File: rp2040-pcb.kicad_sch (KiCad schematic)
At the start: 10 parts

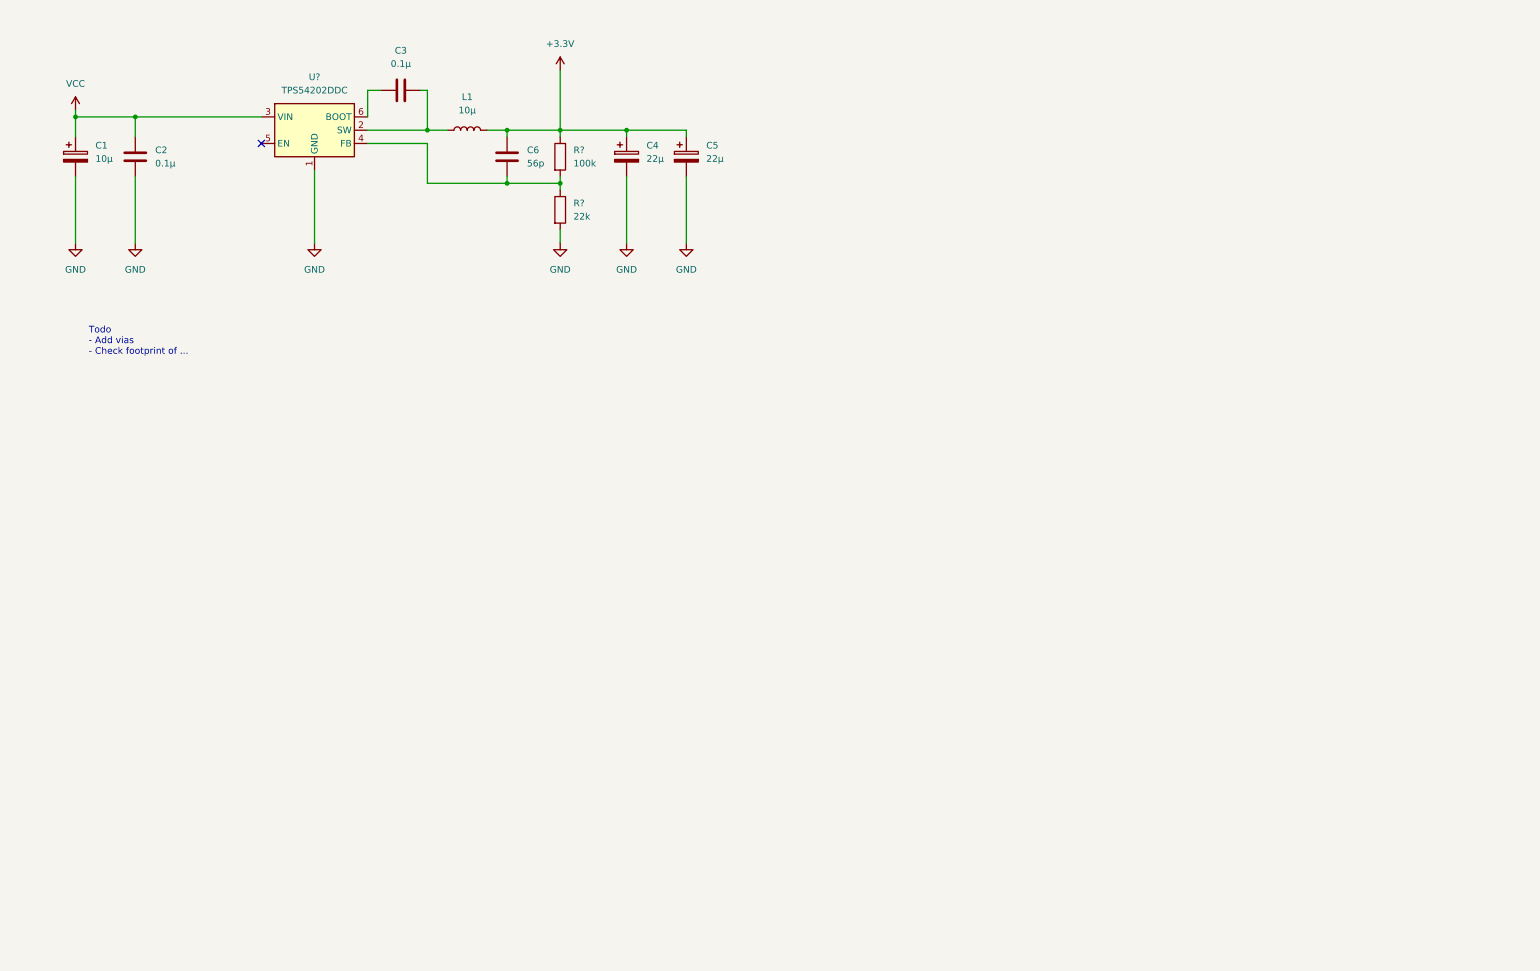
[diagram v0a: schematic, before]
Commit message: Added SPI-memory.
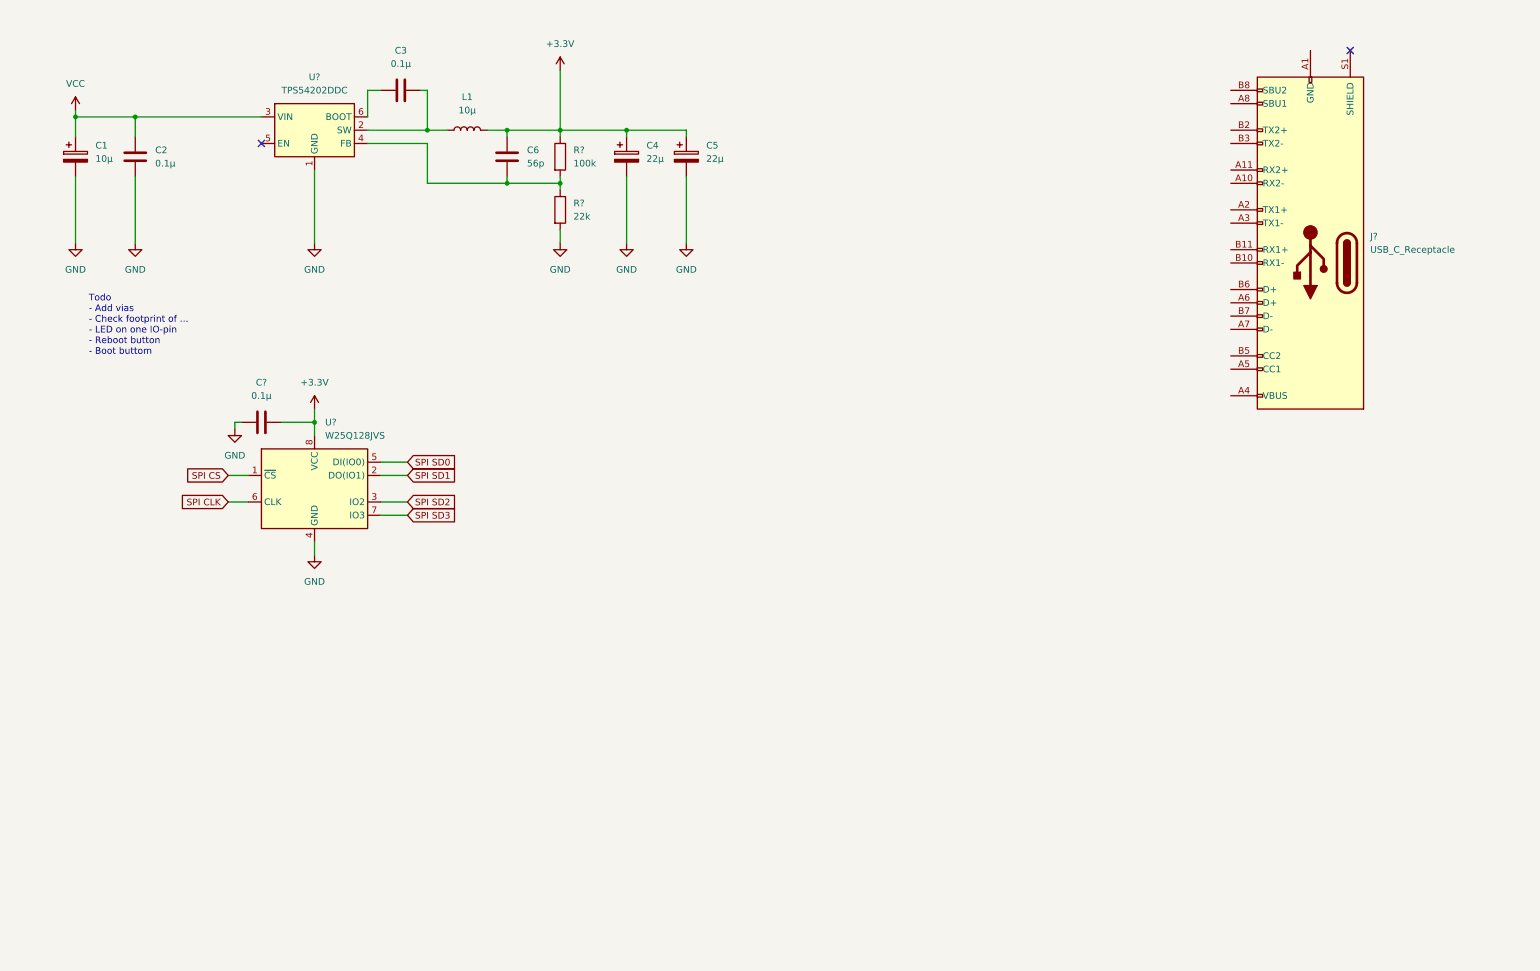
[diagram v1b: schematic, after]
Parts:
- added C?: 0.1µ, Capacitor_SMD:C_0805_2012Metric, symbol Device:C
- added J?: USB_C_Receptacle, symbol Connector:USB_C_Receptacle
- added U?: W25Q128JVS, Package_SO:SOIC-8_5.23x5.23mm_P1.27mm, symbol Memory_Flash:W25Q128JVS
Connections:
- net +3.3V: now also C?.2, U?.8 (VCC)
- net GND: now also C?.1, U?.4 (GND)
- new net: J?.A1 (GND), J?.A12 (GND), J?.B1 (GND), J?.B12 (GND)
- new net: J?.A4 (VBUS), J?.A9 (VBUS), J?.B4 (VBUS), J?.B9 (VBUS)
- new net SPI CLK: U?.6 (CLK)
- new net SPI CS: U?.1 (~{CS})
- new net SPI SD0: U?.5 (DI(IO0))
- new net SPI SD1: U?.2 (DO(IO1))
- new net SPI SD2: U?.3 (IO2)
- new net SPI SD3: U?.7 (IO3)
- no-connect marks 1 -> 2
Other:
- note added: "Todo - Add vias - Check footprint of ... - LED on one IO-pin - Reboot button - Boot buttom"
- note removed: "Todo - Add vias - Check footprint of ..."

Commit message: Added USB, RP2040 and decoupling caps.
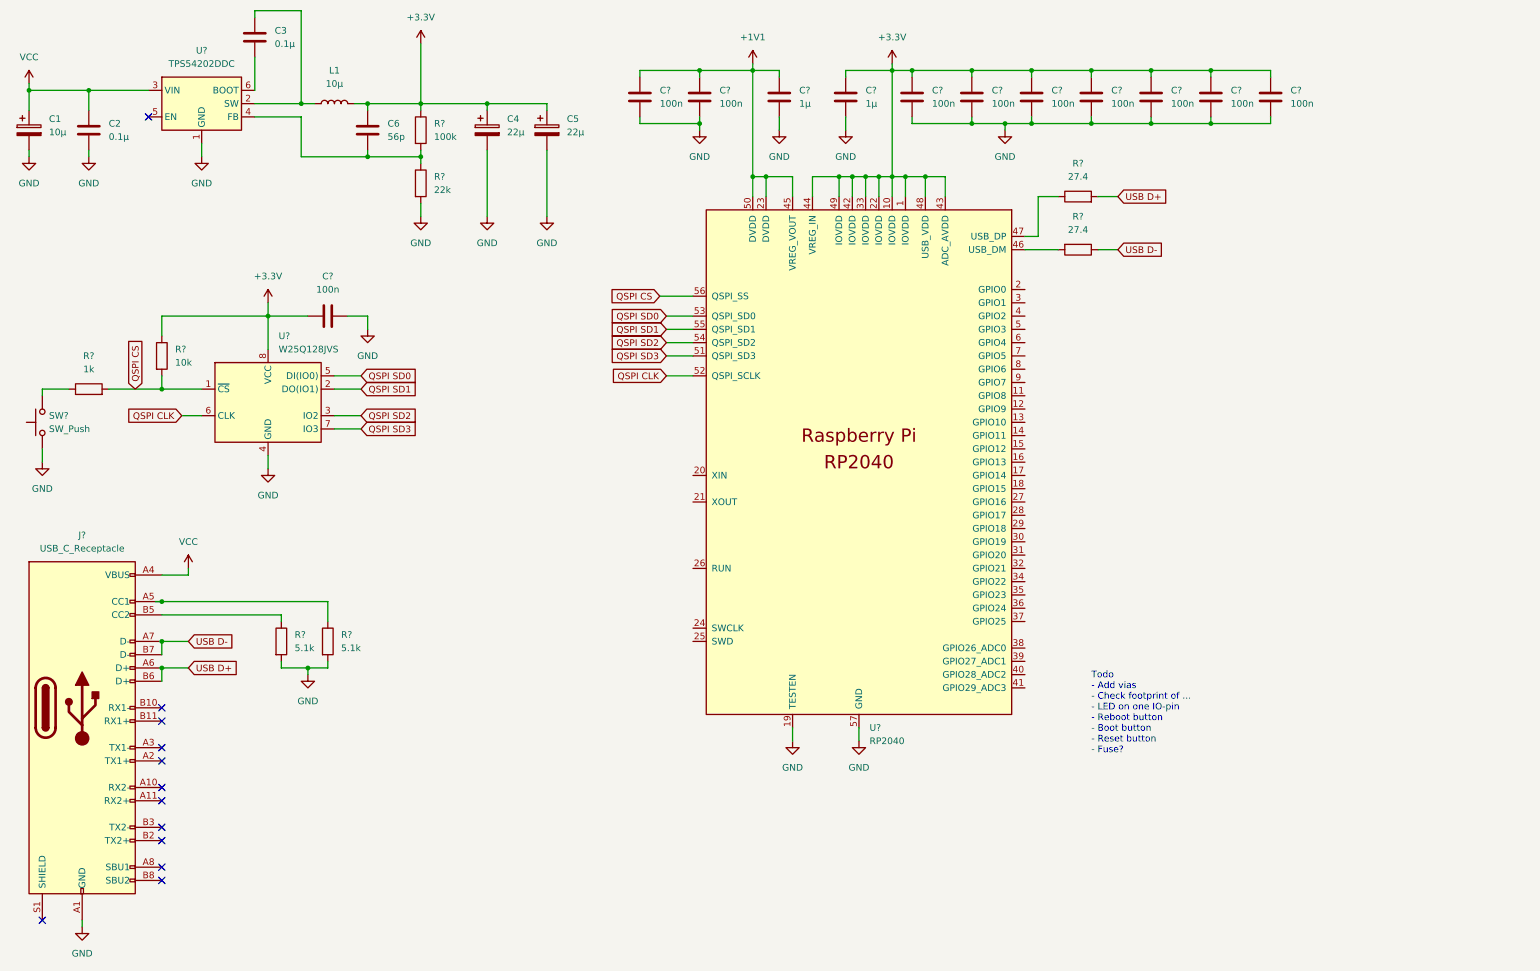
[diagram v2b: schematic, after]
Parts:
- added C? (x2): 1µ, Capacitor_SMD:C_0805_2012Metric, symbol Device:C
- added C? (x9): 100n, Capacitor_SMD:C_0805_2012Metric, symbol Device:C
- added R? (x2): 27.4, symbol Device:R
- added R?: 1k, symbol Device:R
- added R? (x2): 5.1k, symbol Device:R
- added R?: 10k, symbol Device:R
- added SW?: SW_Push, symbol Switch:SW_Push
- added U?: RP2040, RP2040_minimal:RP2040-QFN-56, symbol MCU_RaspberryPi_RP2040:RP2040
- C?: value 0.1µ -> 100n
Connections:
- net +3.3V: now also C?.1, C?.1, C?.1, C?.1, C?.1, C?.1, C?.1, C?.1, R?.1, U?.1 (IOVDD), U?.10 (IOVDD), U?.22 (IOVDD), U?.33 (IOVDD), U?.42 (IOVDD), U?.43 (ADC_AVDD), U?.44 (VREG_IN), U?.48 (USB_VDD), U?.49 (IOVDD)
- net GND: now also J?.A1 (GND), J?.A12 (GND), J?.B1 (GND), J?.B12 (GND), C?.2, C?.2, C?.2, C?.2, C?.2, C?.2, C?.2, C?.2, C?.2, C?.2, C?.2, R?.2, R?.2, SW?.1, U?.19 (TESTEN), U?.57 (GND)
- net VCC: now also J?.A4 (VBUS), J?.A9 (VBUS), J?.B4 (VBUS), J?.B9 (VBUS)
- net at J?.A5 (CC1): now also R?.1
- net USB D+: now reaches J?.A6 (D+)
- net USB D+: now also J?.B6 (D+), R?.2
- net USB D-: now reaches J?.A7 (D-)
- net USB D-: now also J?.B7 (D-), R?.1
- net at J?.B5 (CC2): now also R?.1
- net SPI CLK renamed QSPI CLK
- net QSPI CLK: now also U?.52 (QSPI_SCLK)
- net SPI CS renamed QSPI CS
- net QSPI CS: now also R?.2, R?.2, U?.56 (QSPI_SS)
- net SPI SD0 renamed QSPI SD0
- net QSPI SD0: now also U?.53 (QSPI_SD0)
- net SPI SD1 renamed QSPI SD1
- net QSPI SD1: now also U?.55 (QSPI_SD1)
- net SPI SD2 renamed QSPI SD2
- net QSPI SD2: now also U?.54 (QSPI_SD2)
- net SPI SD3 renamed QSPI SD3
- net QSPI SD3: now also U?.51 (QSPI_SD3)
- new net: R?.1, SW?.2
- new net: R?.1, U?.47 (USB_DP)
- new net: R?.2, U?.46 (USB_DM)
- new net +1V1: C?.1, C?.1, C?.1, U?.23 (DVDD), U?.45 (VREG_VOUT), U?.50 (DVDD)
- no-connect marks 2 -> 12
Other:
- note added: "Todo - Add vias - Check footprint of ... - LED on one IO-pin - Reboot button - Boot button - Reset button - Fuse?"
- note removed: "Todo - Add vias - Check footprint of ... - LED on one IO-pin - Reboot button - Boot buttom"
- moved on the sheet: C1, C2, C3, C4, C5, C6, C?, J?, L1, R?, U?

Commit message: Added IO-header-pins.
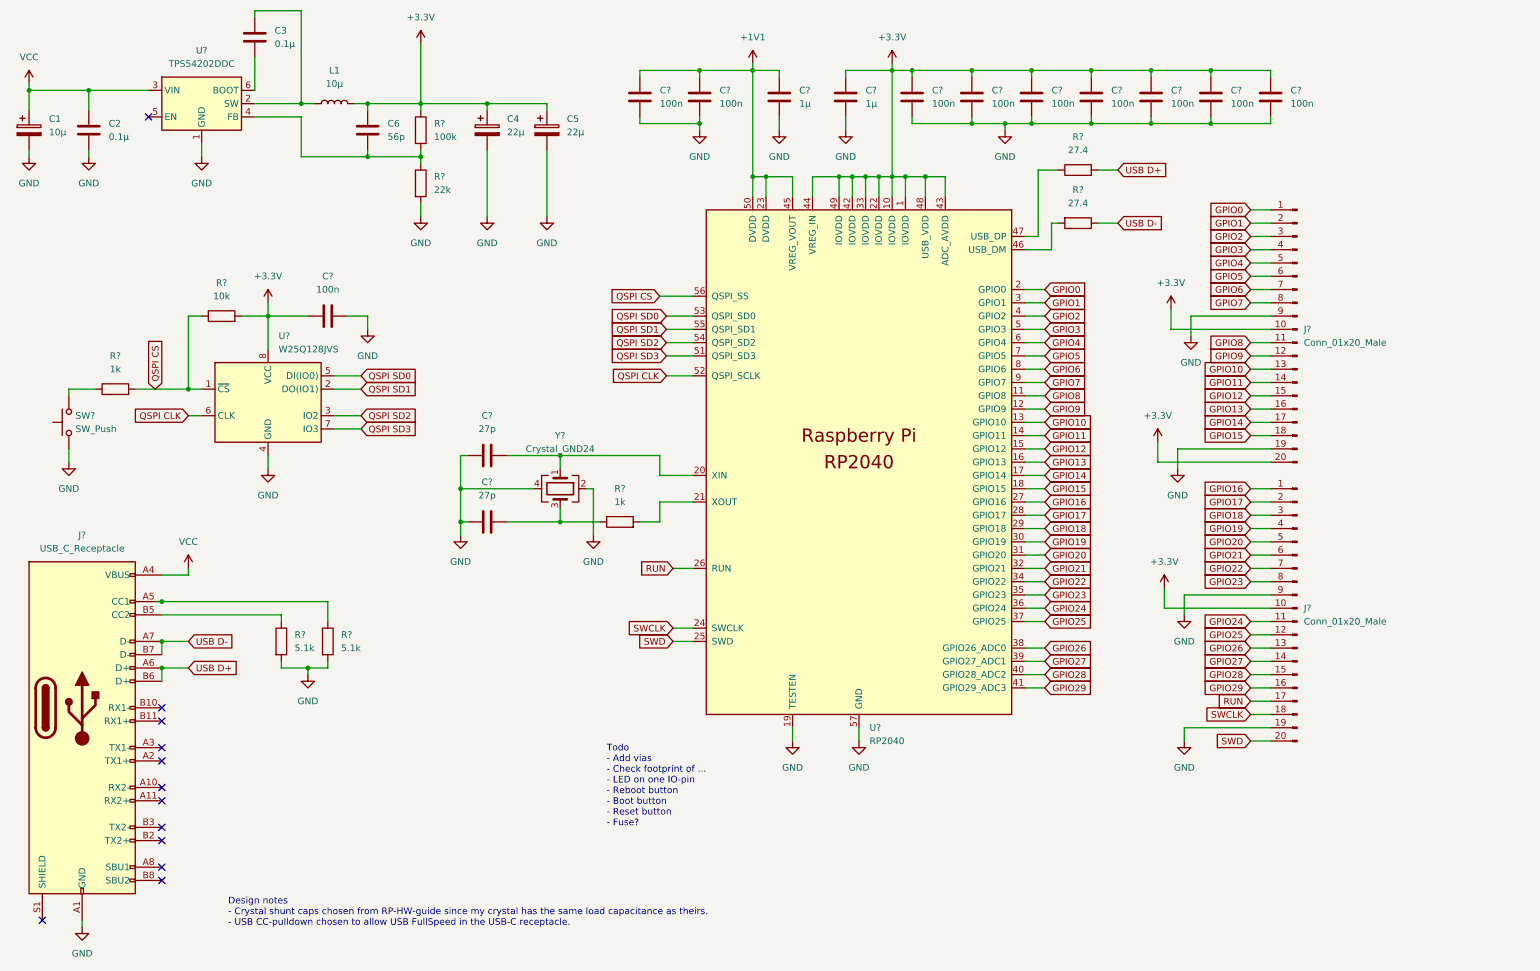
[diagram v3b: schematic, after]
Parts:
- added C? (x2): 27p, Capacitor_SMD:C_0805_2012Metric, symbol Device:C
- added J? (x2): Conn_01x20_Male, symbol Connector:Conn_01x20_Male
- added R?: 1k, symbol Device:R
- added Y?: Crystal_GND24, symbol Device:Crystal_GND24
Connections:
- net +3.3V: now also R?.2, J?.10 (Pin_10), J?.10 (Pin_10), J?.20 (Pin_20); no longer R?.1
- net GND: now also C?.1, C?.1, J?.19 (Pin_19), J?.19 (Pin_19), J?.9 (Pin_9), J?.9 (Pin_9), Y?.2, Y?.4
- net QSPI CS: now also R?.1; no longer R?.2
- net GPIO8: now reaches U?.11 (GPIO8)
- net GPIO8: now also J?.11 (Pin_11)
- net GPIO9: now reaches U?.12 (GPIO9)
- net GPIO9: now also J?.12 (Pin_12)
- net GPIO10: now reaches U?.13 (GPIO10)
- net GPIO10: now also J?.13 (Pin_13)
- net GPIO11: now reaches U?.14 (GPIO11)
- net GPIO11: now also J?.14 (Pin_14)
- net GPIO12: now reaches U?.15 (GPIO12)
- net GPIO12: now also J?.15 (Pin_15)
- net GPIO13: now reaches U?.16 (GPIO13)
- net GPIO13: now also J?.16 (Pin_16)
- net GPIO14: now reaches U?.17 (GPIO14)
- net GPIO14: now also J?.17 (Pin_17)
- net GPIO15: now reaches U?.18 (GPIO15)
- net GPIO15: now also J?.18 (Pin_18)
- net GPIO0: now reaches U?.2 (GPIO0)
- net GPIO0: now also J?.1 (Pin_1)
- net at U?.20 (XIN): now also C?.2, Y?.1
- net at U?.21 (XOUT): now also R?.2
- net SWCLK: now reaches U?.24 (SWCLK)
- net SWCLK: now also J?.18 (Pin_18)
- net SWD: now reaches U?.25 (SWD)
- net SWD: now also J?.20 (Pin_20)
- net RUN: now reaches U?.26 (RUN)
- net RUN: now also J?.17 (Pin_17)
- net GPIO16: now reaches U?.27 (GPIO16)
- net GPIO16: now also J?.1 (Pin_1)
- net GPIO17: now reaches U?.28 (GPIO17)
- net GPIO17: now also J?.2 (Pin_2)
- net GPIO18: now reaches U?.29 (GPIO18)
- net GPIO18: now also J?.3 (Pin_3)
- net GPIO1: now reaches U?.3 (GPIO1)
- net GPIO1: now also J?.2 (Pin_2)
- net GPIO19: now reaches U?.30 (GPIO19)
- net GPIO19: now also J?.4 (Pin_4)
- net GPIO20: now reaches U?.31 (GPIO20)
- net GPIO20: now also J?.5 (Pin_5)
- net GPIO21: now reaches U?.32 (GPIO21)
- net GPIO21: now also J?.6 (Pin_6)
- net GPIO22: now reaches U?.34 (GPIO22)
- net GPIO22: now also J?.7 (Pin_7)
- net GPIO23: now reaches U?.35 (GPIO23)
- net GPIO23: now also J?.8 (Pin_8)
- net GPIO24: now reaches U?.36 (GPIO24)
- net GPIO24: now also J?.11 (Pin_11)
- net GPIO25: now reaches U?.37 (GPIO25)
- net GPIO25: now also J?.12 (Pin_12)
- net GPIO26: now reaches U?.38 (GPIO26_ADC0)
- net GPIO26: now also J?.13 (Pin_13)
- net GPIO27: now reaches U?.39 (GPIO27_ADC1)
- net GPIO27: now also J?.14 (Pin_14)
- net GPIO2: now reaches U?.4 (GPIO2)
- net GPIO2: now also J?.3 (Pin_3)
- net GPIO28: now reaches U?.40 (GPIO28_ADC2)
- net GPIO28: now also J?.15 (Pin_15)
- net GPIO29: now reaches U?.41 (GPIO29_ADC3)
- net GPIO29: now also J?.16 (Pin_16)
- net GPIO3: now reaches U?.5 (GPIO3)
- net GPIO3: now also J?.4 (Pin_4)
- net GPIO4: now reaches U?.6 (GPIO4)
- net GPIO4: now also J?.5 (Pin_5)
- net GPIO5: now reaches U?.7 (GPIO5)
- net GPIO5: now also J?.6 (Pin_6)
- net GPIO6: now reaches U?.8 (GPIO6)
- net GPIO6: now also J?.7 (Pin_7)
- net GPIO7: now reaches U?.9 (GPIO7)
- net GPIO7: now also J?.8 (Pin_8)
- new net: C?.2, R?.1, Y?.3
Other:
- note added: "Design notes - Crystal shunt caps chosen from RP-HW-guide since my crystal has the same load capacitance as theirs. - USB CC-pulldown chosen to allow USB FullSpeed in the USB-C receptacle."
- moved on the sheet: R?, SW?
